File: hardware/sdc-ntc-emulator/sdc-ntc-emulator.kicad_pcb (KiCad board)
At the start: 2 copper layers, 104 x 76 mm, 37 parts, among them J1 DevKit J1, J2 DevKit J3, J3 5V IN (RAC03), J4 SDC VE1 / GND, K1 G5V-2-H1 5VDC, Q1 AO3400A, Q2 AO3401A, U1 ISO1540, U2 AD5272BRMZ-50

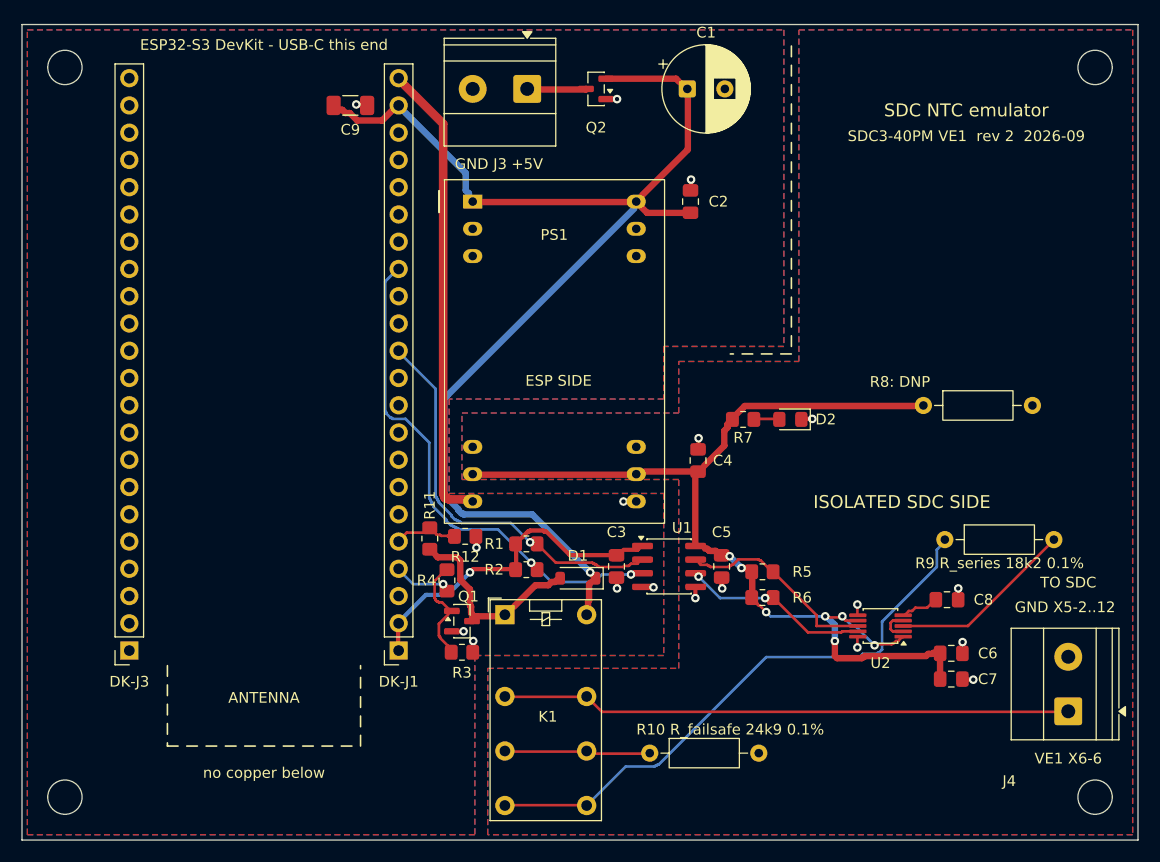
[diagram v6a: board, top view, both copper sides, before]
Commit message: PCB rev 3: TMR 1-0511 isolated supply, DigiKey-verified BOM
- PS1 Traco TMR 1-0511 (SIP-6) replaces the TEM 2-0511; straight isolation gap >= 1.40 mm
- Parts that were obsolete, backordered or not stocked at DigiKey replaced by stocked equivalents
- DigiKey upload file carries DigiKey part numbers; quantities follow DigiKey price breaks, spares only where useful

Co-Authored-By: Claude Opus 5.5 <noreply@anthropic.com>
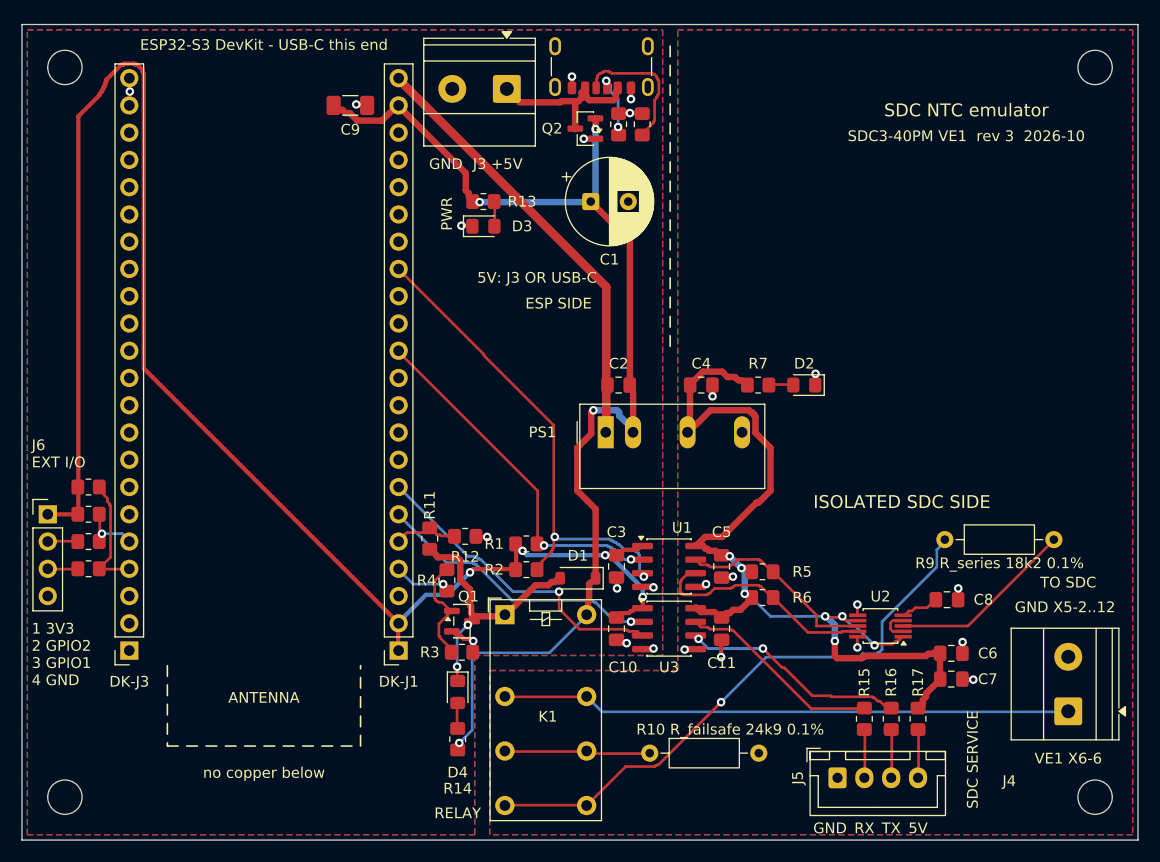
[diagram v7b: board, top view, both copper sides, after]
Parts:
- removed R8: 270R 0.6W, Resistor_THT:R_Axial_DIN0207_L6.3mm_D2.5mm_P10.16mm_Horizontal
- added C10: 100nF, Capacitor_SMD:C_0805_2012Metric_Pad1.18x1.45mm_HandSolder, F.Cu at (155.4, 106.3)
- added C11: 100nF, Capacitor_SMD:C_0805_2012Metric_Pad1.18x1.45mm_HandSolder, F.Cu at (165.2, 106.3)
- added D3: green, LED_SMD:LED_0805_2012Metric_Pad1.15x1.40mm_HandSolder, F.Cu at (143.0, 68.8)
- added D4: yellow, LED_SMD:LED_0805_2012Metric_Pad1.15x1.40mm_HandSolder, F.Cu at (140.6, 112.2)
- added J5: SDC SERVICE, Connector_JST:JST_XH_B4B-XH-A_1x04_P2.50mm_Vertical, F.Cu at (176.0, 120.2)
- added J6: EXT I/O, Connector_PinHeader_2.54mm:PinHeader_1x04_P2.54mm_Vertical, F.Cu at (102.4, 95.6)
- added J7: USB-C 5V IN, Connector_USB:USB_C_Receptacle_GCT_USB4125-xx-x-0190_6P_TopMnt_Horizontal, F.Cu at (154.0, 52.8)
- added R13: 2k2, Resistor_SMD:R_0805_2012Metric_Pad1.20x1.40mm_HandSolder, F.Cu at (143.0, 66.5)
- added R14: 2k2, Resistor_SMD:R_0805_2012Metric_Pad1.20x1.40mm_HandSolder, F.Cu at (140.6, 116.6)
- added R15: 1k, Resistor_SMD:R_0805_2012Metric_Pad1.20x1.40mm_HandSolder, F.Cu at (178.5, 114.7)
- added R16: 1k, Resistor_SMD:R_0805_2012Metric_Pad1.20x1.40mm_HandSolder, F.Cu at (181.0, 114.7)
- added R17: 0R, Resistor_SMD:R_0805_2012Metric_Pad1.20x1.40mm_HandSolder, F.Cu at (183.5, 114.7)
- added R18: 100R, Resistor_SMD:R_0805_2012Metric_Pad1.20x1.40mm_HandSolder, F.Cu at (106.2, 98.2)
- added R19: 100R, Resistor_SMD:R_0805_2012Metric_Pad1.20x1.40mm_HandSolder, F.Cu at (106.2, 100.7)
- added R20: 4k7, Resistor_SMD:R_0805_2012Metric_Pad1.20x1.40mm_HandSolder, F.Cu at (106.2, 95.6)
- added R21: 4k7, Resistor_SMD:R_0805_2012Metric_Pad1.20x1.40mm_HandSolder, F.Cu at (106.2, 93.1)
- added R22: 5k1, Resistor_SMD:R_0805_2012Metric_Pad1.20x1.40mm_HandSolder, F.Cu at (155.6, 59.3)
- added R23: 5k1, Resistor_SMD:R_0805_2012Metric_Pad1.20x1.40mm_HandSolder, F.Cu at (157.8, 59.3)
- added U3: ISO7721D, Package_SO:SOIC-8_3.9x4.9mm_P1.27mm, F.Cu at (160.3, 106.3)
- C2: value 100nF -> 10uF 16V X5R
- PS1: value TEM 2-0511 -> TMR 1-0511; footprint sdc_emulator:Traco_TEM2_Single_DIP24 -> Converter_DCDC:Converter_DCDC_TRACO_TMR-1-xxxx_Single_THT
- moved PS1 24.8 mm to (154.4, 88.0)
- moved C2 18.4 mm to (155.6, 83.6), turned to 180 degrees
- moved C1 13.8 mm to (153.0, 66.5)
- moved C4 7.04 mm to (163.3, 83.6), turned to 0 degrees
- moved Q2 3.83 mm to (152.5, 59.7)
- moved R7 3.49 mm to (168.6, 83.6)
- moved D2 3.45 mm to (172.9, 83.6)
- moved J3 1.90 mm to (145.2, 56.0)
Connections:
- J1 pad 6: unconnected-(J1-Pin_6-Pad6) -> /SVC_RX
- J1 pad 7: unconnected-(J1-Pin_7-Pad7) -> /SVC_TX
- J2 pad 4: unconnected-(J2-Pin_4-Pad4) -> /EXT_IO1
- J2 pad 5: unconnected-(J2-Pin_5-Pad5) -> /EXT_IO2
- PS1 pad 1: /+5V -> /GND
- PS1 pad 2: unconnected-(PS1-NC-Pad2) -> /+5V
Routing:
- net /+3V3: track 28.3 -> 144.1 mm, vias 1 -> 4
- net /SVC_TX: track 0.00 -> 28.7 mm, vias 0 -> 1
- net /SVC_RX: track 0.00 -> 26.1 mm, vias 0 -> 1
- net /SVC_TX_ISO: track 0.00 -> 20.9 mm, vias 0 -> 2
- net /SVC_RX_ISO: track 0.00 -> 18.8 mm
- net /USB_CC2: track 0.00 -> 12.7 mm
- net /EXT_IO1: track 0.00 -> 9.85 mm
- net /+5V_IN: track 4.25 -> 13.7 mm
- net /+5V: track 110.3 -> 101.4 mm, vias 1 -> 4
- net /VDD_ISO: track 88.7 -> 81.7 mm
- net /COIL_N: track 17.0 -> 22.8 mm, vias 0 -> 2
- net /USB_CC1: track 0.00 -> 5.63 mm, vias 0 -> 2
- net /GND: track 53.8 -> 58.4 mm, vias 9 -> 13
- net /EXT_IO2: track 0.00 -> 4.43 mm, vias 0 -> 1
- net /SVC_TX_EXT: track 0.00 -> 4.07 mm
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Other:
- board text added: "1 3V3"
- board text added: "2 GPIO2"
- board text added: "3 GPIO1"
- board text added: "4 GND"
- board text added: "5V"
- board text added: "5V: J3 OR USB-C"
- board text added: "EXT I/O"
- board text added: "J6"
- board text added: "PWR"
- board text added: "RELAY"
- board text added: "RX"
- board text added: "SDC SERVICE"
- board text added: "SDC3-40PM VE1 rev 3 2026-10"
- board text added: "TX"
- board text removed: "R8: DNP"
- board text removed: "SDC3-40PM VE1 rev 2 2026-09"
